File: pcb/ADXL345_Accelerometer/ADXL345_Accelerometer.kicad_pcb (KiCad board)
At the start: 2 copper layers, 25.4 x 22.9 mm, 16 parts, among them J1 Conn_01x09, Q1 BSS138, Q2 BSS138, U1 ADXL345_Library, U2 AP2112K-3.3

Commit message: Correcciones
Se corrigieron segun las recomendaciones realizadas por el docente.
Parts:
- U1: value ADXL345_Library -> ADXL345
- moved Q2 4.68 mm to (148.6, 87.6), turned to 180 degrees
- moved R2 4.06 mm to (151.4, 90.3), turned to 270 degrees
- moved R3 3.38 mm to (151.6, 97.1), turned to 180 degrees
- moved U1 2.72 mm to (143.6, 91.5)
- moved R5 2.69 mm to (152.3, 94.0), turned to 270 degrees
- moved C1 2.52 mm to (138.2, 88.6), turned to 180 degrees
- moved Q1 2.36 mm to (149.6, 94.5)
- moved R4 2.34 mm to (139.2, 91.3), turned to 270 degrees
- moved D1 1.84 mm to (142.8, 96.6), turned to 180 degrees
- moved R6 1.81 mm to (136.3, 91.5), turned to 90 degrees
- moved U2 1.56 mm to (137.8, 95.9)
- moved R1 1.22 mm to (148.8, 91.1), turned to 90 degrees
- moved C2 0.79 mm to (133.3, 95.9)
- moved J1 0.23 mm to (134.0, 101.3)
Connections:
- net /SDA\SDIO_3V renamed Net-(Q1-Pad2)
- C1 pad 1: +3V3 -> Net-(C1-Pad1)
- J1 pad 2: +3V3 -> Net-(C1-Pad1)
- Q2 pad 2: /SCL_3V -> /SCL
- Q2 pad 3: /SCL -> /SCL_3V
- R2 pad 1: +3V3 -> /SCL_3V
- R2 pad 2: /SCL_3V -> +3V3
- R4 pad 1: +3V3 -> Net-(C1-Pad1)
- R5 pad 1: /VIN -> /SCL
- R5 pad 2: /SCL -> /VIN
- U1 pad 1: +3V3 -> Net-(C1-Pad1)
- U1 pad 6: +3V3 -> Net-(C1-Pad1)
- U2 pad 5: +3V3 -> Net-(C1-Pad1)
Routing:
- net +3V3: track 67.4 -> 7.55 mm, vias 2 -> 0
- net Net-(C1-Pad1): track 0.00 -> 28.5 mm
- net /SDO\ADDR: track 44.7 -> 26.7 mm
- net /SCL_3V: track 9.29 -> 18.1 mm, vias 0 -> 2
- net /SCL: track 11.6 -> 19.7 mm, vias 2 -> 0
- net /VIN: track 42.5 -> 35.7 mm, vias 0 -> 2
- net GND: track 17.3 -> 20.8 mm, vias 5 -> 3
- net /SDA\SDIO: track 10.2 -> 7.64 mm
- net /INT2: track 12.8 -> 11.3 mm
- net /CS: track 6.42 -> 5.52 mm
- net Net-(Q1-Pad2): track 8.53 -> 9.15 mm
- net /INT1: track 11.9 -> 11.3 mm
- added copper zone on B.Cu, net GND
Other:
- net class Alimentacion: clearance 0.2 -> 0.4
- net class Default: clearance 0.2 -> 0.4
- rule trace_clearance: 0.2 -> 0.4

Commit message: Update ADXL345_Accelerometer.kicad_pcb
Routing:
- added copper zone on F.Cu, net /VIN

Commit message: Correcciones
Se corrigieron detalles y se agregaron códigos de catálogo recomendados.
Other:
- board text added: "Designed In Argentina"
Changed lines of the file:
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@@
   (general
     (thickness 1.6)
-    (drawings 38)
+    (drawings 39)
     (tracks 155)
     (zones 0)
@@
     (47 F.CrtYd user)
     (48 B.Fab user)
-    (49 F.Fab user hide)
+    (49 F.Fab user)
   )
   (setup
@@
     )
   )
+  (gr_text "Designed In \nArgentina" (at 141.24 92.64) (layer B.SilkS)
+    (effects (font (size 1.2 1.2) (thickness 0.15)) (justify mirror))
+  )
   (gr_poly (pts (xy 148.795 102.73) (xy 149.765 102.73) (xy 149.78 102.76) (xy 149.28 103.31)) (layer F.SilkS) (width 0.1))

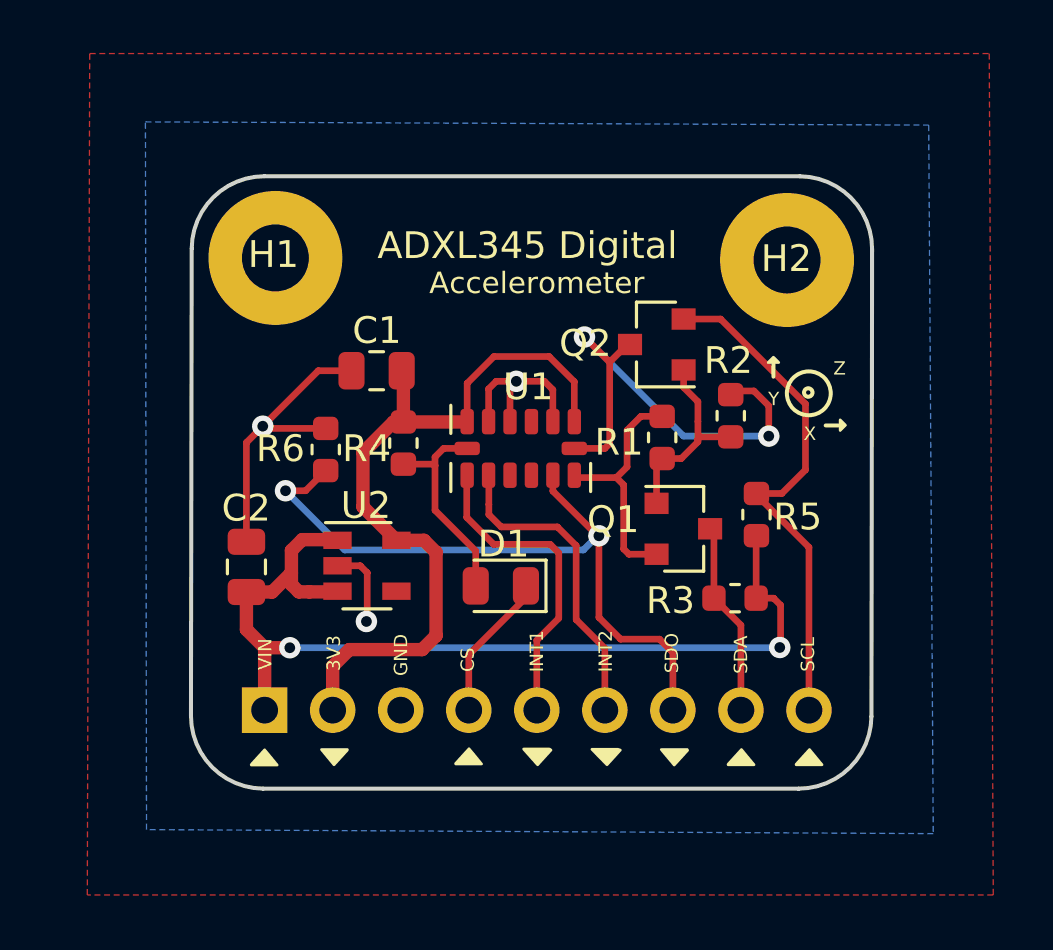
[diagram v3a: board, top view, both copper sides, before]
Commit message: Se agregaron fiduciales
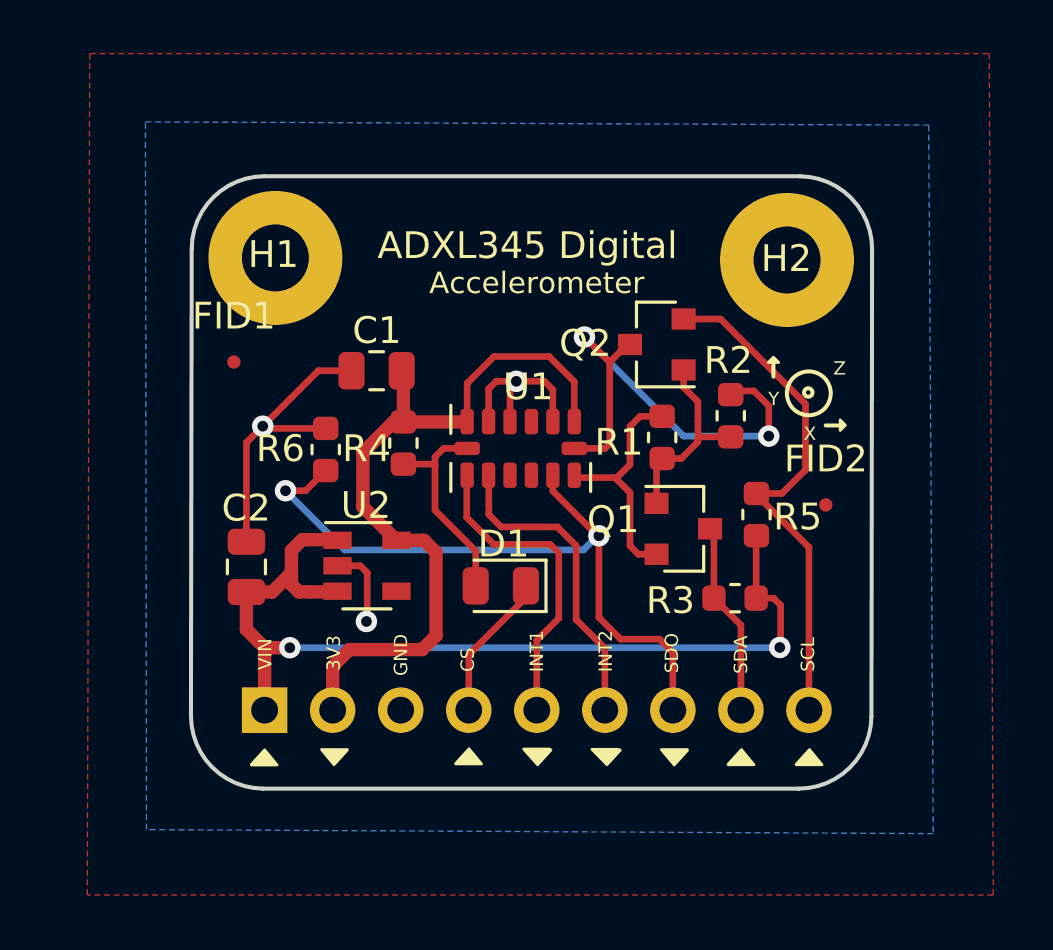
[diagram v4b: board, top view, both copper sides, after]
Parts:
- added FID1: Fiducial, Fiducial:Fiducial_0.5mm_Mask1.5mm, F.Cu at (132.8, 88.3)
- added FID2: Fiducial, Fiducial:Fiducial_0.5mm_Mask1.5mm, F.Cu at (154.9, 93.6)
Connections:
- net /SCL_3V renamed Net-(Q2-Pad3)
- net /SDA\SDIO renamed /SDA
- net /SDO\ADDR renamed /SDO
- C1 pad 1: Net-(C1-Pad1) -> +3V3
- J1 pad 2: Net-(C1-Pad1) -> +3V3
- R4 pad 1: Net-(C1-Pad1) -> +3V3
- U1 pad 1: Net-(C1-Pad1) -> +3V3
- U1 pad 6: Net-(C1-Pad1) -> +3V3
- U2 pad 5: Net-(C1-Pad1) -> +3V3
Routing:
- net Net-(C1-Pad1): track 28.4 -> 0.00 mm
- net +3V3: track 7.52 -> 35.9 mm
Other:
- board text added: "Grilla: 0,5 mm Ancho de las pistas: 0,25 mm Ancho de via: 0,25 mm Ancho de agujero: 2,5 mm"

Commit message: Correcciones
Se hicieron las correcciones de acuerdo a las recomendaciones del docente.
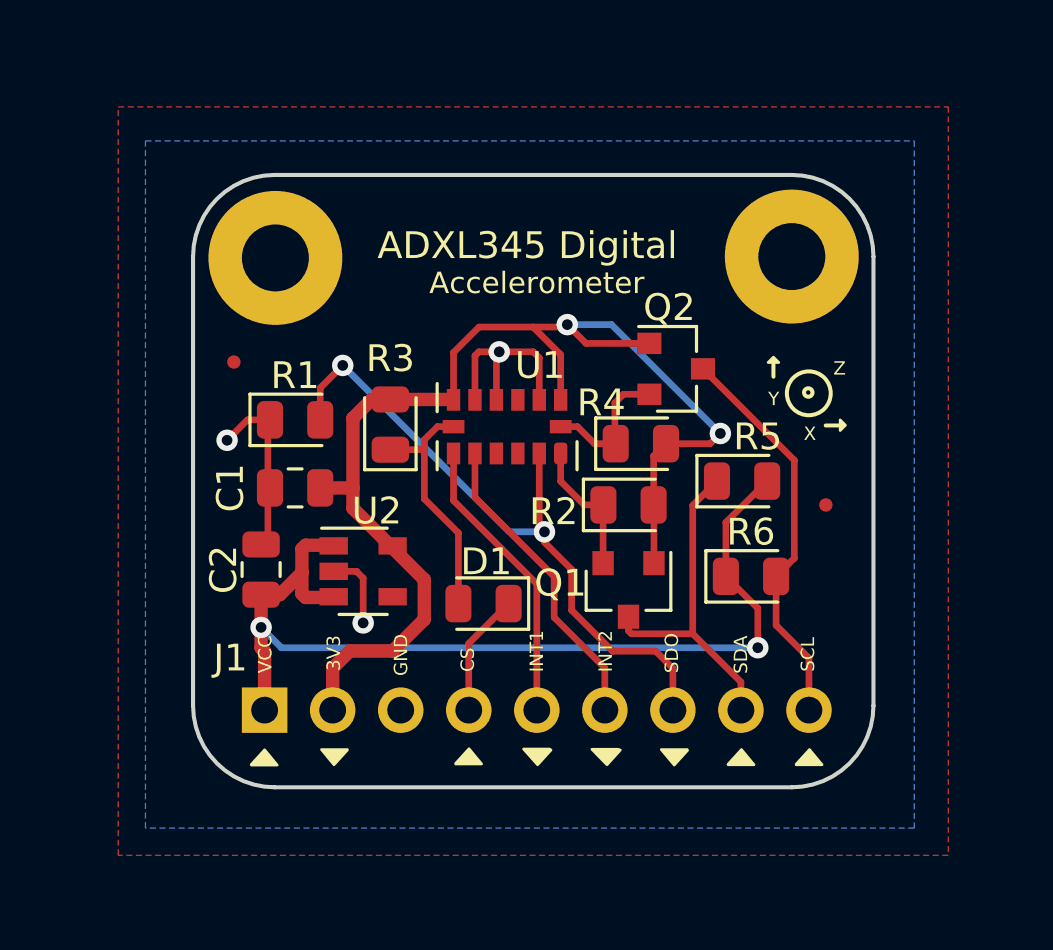
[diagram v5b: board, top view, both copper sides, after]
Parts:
- R1, R2, R3, R4, R5, R6: footprint Resistor_SMD:R_0603_1608Metric -> Diode_SMD:D_0805_2012Metric
- U1: value ADXL345 -> ADXL345BCCZ
- moved R6 16.6 mm to (152.1, 96.3), turned to 0 degrees
- moved R3 14.4 mm to (138.7, 90.6), turned to 90 degrees
- moved R1 13.7 mm to (135.1, 90.4), turned to 0 degrees
- moved R4 8.86 mm to (148.0, 91.3), turned to 0 degrees
- moved C1 5.33 mm to (135.1, 93.0), turned to 0 degrees
- moved R2 5.06 mm to (147.6, 93.6), turned to 0 degrees
- moved Q1 3.07 mm to (147.6, 96.8), turned to 270 degrees
- moved R5 1.36 mm to (151.8, 92.7), turned to 0 degrees
- moved Q2 1.16 mm to (149.4, 88.5), turned to 0 degrees
- moved U1 0.96 mm to (143.0, 90.7)
- moved D1 0.92 mm to (142.2, 97.3)
- moved C2 0.56 mm to (133.9, 96.0)
- moved U2 0.25 mm to (137.7, 96.1)
- moved H2 0.22 mm to (153.7, 84.3)
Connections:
- C1 pad 1: +3V3 -> GND
- C1 pad 2: GND -> +3V3
- C2 pad 1: /VIN -> VCC
- J1 pad 1: /VIN -> VCC
- Q2 pad 2: /SCL -> Net-(Q2-Pad2)
- Q2 pad 3: Net-(Q2-Pad3) -> /SCL
- R1 pad 1: +3V3 -> GND
- R1 pad 2: Net-(Q1-Pad2) -> /SDO
- R2 pad 1: Net-(Q2-Pad3) -> Net-(Q1-Pad2)
- R3 pad 1: /VIN -> Net-(D1-Pad2)
- R3 pad 2: /SDA -> +3V3
- R4 pad 1: +3V3 -> Net-(Q2-Pad2)
- R4 pad 2: Net-(D1-Pad2) -> +3V3
- R5 pad 1: /SCL -> /SDA
- R5 pad 2: /VIN -> VCC
- R6 pad 1: /SDO -> VCC
- R6 pad 2: GND -> /SCL
- U1 pad 14: Net-(Q2-Pad3) -> Net-(Q2-Pad2)
- U2 pad 1: /VIN -> VCC
- U2 pad 3: /VIN -> VCC
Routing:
- net VCC: track 0.00 -> 36.6 mm, vias 0 -> 2
- net /VIN: track 35.7 -> 0.00 mm, vias 2 -> 0
- net Net-(Q2-Pad3): track 18.0 -> 0.00 mm, vias 2 -> 0
- net +3V3: track 35.9 -> 47.2 mm, vias 0 -> 2
- net /SDA: track 7.18 -> 12.6 mm
- net Net-(Q2-Pad2): track 0.00 -> 5.27 mm
- net /SCL: track 19.4 -> 14.9 mm
- net GND: track 20.8 -> 16.7 mm
- net Net-(Q1-Pad2): track 9.01 -> 5.18 mm
- net Net-(D1-Pad2): track 7.97 -> 9.24 mm
- net /SDO: track 26.2 -> 25.2 mm
- net /CS: track 5.52 -> 4.59 mm
- added copper zone on F.Cu, net VCC
- removed copper zone on F.Cu, net /VIN
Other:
- outline, holes or cut-outs redrawn
- board text added: "Grilla: 0,5 mm Ancho de las pistas: 0,25 mm Diametro de via: 0,80 mm Ancho de agujero: 0,40 mm"
- board text added: "VCC"
- board text removed: "Grilla: 0,5 mm Ancho de las pistas: 0,25 mm Ancho de via: 0,25 mm Ancho de agujero: 2,5 mm"
- board text removed: "VIN"

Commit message: Modelos 3D del proyecto
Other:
- board text added: "Diseñado en Argentina"
- board text added: "Grilla: 0,5 mm Ancho de las pistas: 0,25 mm Via: 0,80 mm ( 0,40 mm ) Margen: 0.40 mm Terminación: HASL"
- board text removed: "Designed In Argentina"
- board text removed: "Grilla: 0,5 mm Ancho de las pistas: 0,25 mm Diametro de via: 0,80 mm Ancho de agujero: 0,40 mm"
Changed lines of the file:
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@@
     (thickness 1.6)
     (drawings 43)
-    (tracks 131)
+    (tracks 130)
     (zones 0)
     (modules 18)
@@
   )
   (setup
-    (last_trace_width 0.25)
+    (last_trace_width 0.5)
     (user_trace_width 0.5)
     (trace_clearance 0.4)
@@
     (descr "Through hole straight pin header, 1x09, 2.54mm pitch, single row")
     (tags "Through hole pin header THT 1x09 2.54mm single row")
-    (fp_text reference J1 (at -1.946 1.275) (layer F.SilkS)
+    (fp_text reference J1 (at -1.946 1.021) (layer F.SilkS)
       (effects (font (size 1 1) (thickness 0.15)))
     )
@@
     (tags capacitor)
     (attr smd)
-    (fp_text reference C2 (at 0 -1.397 270) (layer F.SilkS)
+    (fp_text reference C2 (at 0 -1.27 90) (layer F.SilkS)
       (effects (font (size 1 1) (thickness 0.15)))
     )
@@
     (tags SOT-23)
     (attr smd)
-    (fp_text reference Q1 (at -0.254 2.54) (layer F.SilkS)
+    (fp_text reference Q1 (at -0.254 2.413 90) (layer F.SilkS)
       (effects (font (size 1 1) (thickness 0.15)))
     )
@@
     (tags diode)
     (attr smd)
-    (fp_text reference R2 (at -2.794 0.254) (layer F.SilkS)
+    (fp_text reference R2 (at -2.413 0 90) (layer F.SilkS)
       (effects (font (size 1 1) (thickness 0.15)))
     )
@@
     (tags diode)
     (attr smd)
-    (fp_text reference R3 (at 2.4615 0 180) (layer F.SilkS)
+    (fp_text reference R3 (at 2.3345 0 180) (layer F.SilkS)
       (effects (font (size 1 1) (thickness 0.15)))
     )
@@
     (tags capacitor)
     (attr smd)
-    (fp_text reference C1 (at -2.413 0 270) (layer F.SilkS)
+    (fp_text reference C1 (at -2.286 0 180) (layer F.SilkS)
       (effects (font (size 1 1) (thickness 0.15)))
     )
@@
   (gr_arc (start 153.67 84.328) (end 156.718 84.328) (angle -90) (layer Edge.Cuts) (width 0.15))
   (gr_line (start 156.718 101.092) (end 156.718 84.328) (layer Edge.Cuts) (width 0.15))
-  (gr_text "Grilla: 0,5 mm\nAncho de las pistas:  0,25 mm\nDiametro de via: 0,80 mm\nAncho de agujero: 0,40 mm\n" (at 176.276 103.759) (layer Dwgs.User)
+  (gr_text "Grilla: 0,5 mm\nAncho de las pistas:  0,25 mm\nVia: 0,80 mm ( 0,40 mm )\nMargen: 0.40 mm\nTerminación: HASL" (at 176.276 103.759) (layer Dwgs.User)
     (effects (font (size 1 1) (thickness 0.15)) (justify left))
   )
-  (gr_text "Designed In \nArgentina" (at 147.193 96.647) (layer B.SilkS)
+  (gr_text "Diseñado en \nArgentina" (at 143.891 84.328) (layer B.SilkS)
     (effects (font (size 1.2 1.2) (thickness 0.15)) (justify mirror))
   )
@@
   (segment (start 141.986 87.884) (end 141.842 88.028) (width 0.25) (layer F.Cu) (net 2))
   (segment (start 144.242 88.108) (end 144.018 87.884) (width 0.25) (layer F.Cu) (net 2))
-  (segment (start 139.954 91.164498) (end 140.440498 90.678) (width 0.25) (layer F.Cu) (net 3))
   (segment (start 141.224 97.282) (end 141.224 94.645252) (width 0.25) (layer F.Cu) (net 3))
   (segment (start 140.440498 90.678) (end 141.042 90.678) (width 0.25) (layer F.Cu) (net 3))
   (segment (start 141.224 94.645252) (end 139.954 93.375252) (width 0.25) (layer F.Cu) (net 3))
-  (segment (start 138.684 91.537) (end 139.857 91.537) (width 0.25) (layer F.Cu) (net 3))
   (segment (start 139.954 93.375252) (end 139.954 91.44) (width 0.25) (layer F.Cu) (net 3))
-  (segment (start 139.857 91.537) (end 139.954 91.44) (width 0.25) (layer F.Cu) (net 3))
   (segment (start 139.954 91.44) (end 139.954 91.164498) (width 0.25) (layer F.Cu) (net 3))
+  (segment (start 139.581498 91.537) (end 140.006749 91.111749) (width 0.25) (layer F.Cu) (net 3))
+  (segment (start 138.684 91.537) (end 139.581498 91.537) (width 0.25) (layer F.Cu) (net 3))
+  (segment (start 139.954 91.164498) (end 140.006749 91.111749) (width 0.25) (layer F.Cu) (net 3))
+  (segment (start 140.006749 91.111749) (end 140.440498 90.678) (width 0.25) (layer F.Cu) (net 3))
   (segment (start 141.042 93.437808) (end 141.042 91.678) (width 0.25) (layer F.Cu) (net 4))
   (segment (start 144.15 96.545808) (end 141.042 93.437808) (width 0.25) (layer F.Cu) (net 4))
@@
   (segment (start 145.923 93.599) (end 145.042 92.718) (width 0.25) (layer F.Cu) (net 8))
   (segment (start 146.6365 93.599) (end 145.923 93.599) (width 0.25) (layer F.Cu) (net 8))
-  (segment (start 146.624 93.6115) (end 146.6365 93.599) (width 0.25) (layer F.Cu) (net 8))
   (segment (start 146.624 95.774) (end 146.624 93.6115) (width 0.25) (layer F.Cu) (net 8))
   (via (at 136.906 88.392) (size 0.8) (drill 0.4) (layers F.Cu B.Cu) (net 9))
@@
   (segment (start 135.382 96.1255) (end 135.382 95.238998) (width 0.5) (layer F.Cu) (net 11))
   (segment (start 135.382 95.238998) (end 135.517999 95.102999) (width 0.5) (layer F.Cu) (net 11))
-  (segment (start 133.99 101.26) (end 133.99 99.065) (width 0.5) (layer F.Cu) (net 11))
-  (segment (start 133.858 98.933) (end 133.858 96.9495) (width 0.5) (layer F.Cu) (net 11))
-  (segment (start 133.99 99.065) (end 133.858 98.933) (width 0.5) (layer F.Cu) (net 11))
   (segment (start 134.617 98.93) (end 133.858 98.171) (width 0.25) (layer B.Cu) (net 11))
   (segment (start 152.4 98.93) (end 134.617 98.93) (width 0.25) (layer B.Cu) (net 11))
+  (segment (start 133.858 98.171) (end 133.858 96.9495) (width 0.5) (layer F.Cu) (net 11))
+  (segment (start 133.99 98.303) (end 133.858 98.171) (width 0.5) (layer F.Cu) (net 11))
+  (segment (start 133.99 101.26) (end 133.99 98.303) (width 0.5) (layer F.Cu) (net 11))
   (segment (start 148.352 89.469) (end 147.386 89.469) (width 0.25) (layer F.Cu) (net 12))
   (segment (start 147.386 89.469) (end 147.066 89.789) (width 0.25) (layer F.Cu) (net 12))
-  (segment (start 147.066 91.283) (end 147.096 91.313) (width 0.25) (layer F.Cu) (net 12))
   (segment (start 147.066 89.789) (end 147.066 91.283) (width 0.25) (layer F.Cu) (net 12))
   (segment (start 145.042 90.678) (end 145.669 90.678) (width 0.25) (layer F.Cu) (net 12))

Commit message: Modelos 3D
Se generaron los modelos 3D.
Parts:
- moved Q2 0.25 mm to (149.1, 88.5)
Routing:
- net +3V3: track 47.2 -> 45.3 mm
- net GND: track 16.7 -> 16.2 mm
